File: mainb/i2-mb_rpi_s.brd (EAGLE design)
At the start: 110 x 110 mm, 30 parts, among them IC3 DS1307Z, T1 BC337, T2 BC337, X15 C-GRID-03-70543, X9 eth (mb->rpi)

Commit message: zmieniony ksztalt mainb
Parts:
- removed X1, X2, X3, X8: (no value), con-maritex:MICROMATCH-4
- removed X12, X13, X14: (no value), con-ptr500:AK500/3-H
- removed X4, X5, X6: (no value), con-ptr500:AK500/3
- added I2C_1, I2C_2, I2C_3, I2C_4: C-GRID-03-70553, con-molex:70553-03
- added PWR1, PWR2, PWR3: TBMP5103RC-KFV1, con-maritex:TBMP5103RC-KF
- moved U$8 23.3 mm to (20.3, 3.81)
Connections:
- net +12V_OUT: now also PWR1.3, PWR2.3, PWR3.3; no longer X4.3, X5.3, X6.3
- net +5V: now also PWR1.1, PWR2.1, PWR3.1; no longer X4.1, X5.1, X6.1
- net GND: now also I2C_1.3, I2C_2.3, I2C_3.3, I2C_4.3, PWR1.2, PWR2.2, PWR3.2; no longer X1.4, X12.2, X13.2, X14.2, X2.4, X3.4, X4.2, X5.2, X6.2, X8.4
- net SCL: now also I2C_1.2, I2C_2.2, I2C_3.2, I2C_4.2; no longer X1.3, X2.3, X3.3, X8.3
- net SDA: now also I2C_1.1, I2C_2.1, I2C_3.1, I2C_4.1; no longer X1.2, X2.2, X3.2, X8.2
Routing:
- net SDA: track 169.7 -> 28.0 mm
- net SCL: track 169.5 -> 31.6 mm
- net +5V_RPI: track 139.6 -> 2.54 mm, vias 1 -> 0
- net +5V: track 117.3 -> 0.00 mm
- net N$4: track 0.00 -> 88.4 mm
- net +12V_IN: track 64.8 -> 0.00 mm
- net +12V_OUT: track 47.5 -> 0.00 mm
- net TX+: track 24.1 -> 0.00 mm
- net TX-: track 24.0 -> 0.00 mm
- net RX+: track 23.9 -> 0.00 mm
- net RX-: track 23.7 -> 0.00 mm
- net AKU+: track 6.53 -> 0.00 mm
- removed copper zone on layer 1, net GND
- removed copper zone on layer 16, net GND
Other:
- board size 110 x 110 mm -> 110 x 107.6 mm

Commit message: 20-11-13 21:08
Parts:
- moved PWR2 211.1 mm to (26.9, 9.09), flipped to the bottom, turned to 60 degrees
- moved PWR1 153.8 mm to (-5.64, -27.8), flipped to the bottom, turned to 180 degrees
- moved I2C_3 136.5 mm to (8.75, -32.4), flipped to the bottom, turned to 180 degrees
- moved I2C_2 135.5 mm to (-23.7, 23.9), flipped to the bottom, turned to 300 degrees
- moved T2 126.2 mm to (14.2, -7.40), flipped to the bottom, turned to 180 degrees
- moved T1 116.3 mm to (-14.2, 8.00), flipped to the bottom
- moved PWR3 110.6 mm to (-26.9, 9.09), flipped to the bottom, turned to 300 degrees
- moved X15 108.1 mm to (-97.1, -87.0)
- moved R28 62.6 mm to (-13.6, 3.22), turned to 180 degrees
- moved BAT 61.2 mm to (42.1, -5.95), turned to 270 degrees
- moved IC3 61.1 mm to (55.7, -26.9)
- moved U$4 57.0 mm to (-10.2, 8.78), turned to 90 degrees
- moved U$8 49.9 mm to (-25.9, -15.0), turned to 180 degrees
- moved I2C_4 46.2 mm to (23.7, 23.9), flipped to the bottom, turned to 60 degrees
- moved Q2 39.4 mm to (25.9, -32.3)
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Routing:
- net N$4: track 88.4 -> 0.00 mm
- net SCL: track 31.6 -> 0.00 mm
- net SDA: track 28.0 -> 0.00 mm
- net N$3: track 25.2 -> 0.00 mm, vias 1 -> 0
- net GND: track 13.7 -> 0.00 mm, vias 3 -> 5
- net N$6: track 4.46 -> 0.00 mm
- net N$9: track 3.51 -> 0.00 mm
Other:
- board size 110 x 107.6 mm -> 110 x 106.6 mm

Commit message: 21.11.13 23:39
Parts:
- removed X15: C-GRID-03-70543, con-molex:70543-03
- added PWR4: C-GRID-03-70543, con-molex:70543-03
- I2C_1: value C-GRID-03-70553 -> C-GRID-03-70543; device con-molex:70553-03 -> con-molex:70543-03
- moved I2C_1 80.1 mm to (-31.8, -29.0), flipped to the bottom, turned to 270 degrees
- moved R2 43.3 mm to (7.20, -7.20), turned to 180 degrees
- moved R28 42.9 mm to (24.9, -15.8), turned to 90 degrees
- moved T1 42.0 mm to (23.0, -11.4), turned to 90 degrees
- moved R1 39.7 mm to (10.2, -7.20), turned to 180 degrees
- moved IC1 37.9 mm to (7.20, -10.8), turned to 180 degrees
- moved Q2 31.3 mm to (48.9, -11.1), turned to 90 degrees
- moved IC3 21.8 mm to (43.3, -9.06), turned to 90 degrees
- moved R3 8.96 mm to (23.4, -15.8), turned to 90 degrees
- moved U$4 8.81 mm to (-9.50, 0.00)
- moved U$3 7.03 mm to (9.50, 0.00), turned to 270 degrees
- moved T2 5.66 mm to (18.2, -11.4), turned to 90 degrees
- moved X9 3.62 mm to (-9.59, 24.4)
- moved X_ETH 1.60 mm to (0.00, 44.6)
- moved BAT 0.17 mm to (42.2, -5.80)
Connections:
- net +12V_OUT: now also PWR4.3; no longer X15.3
- net +5V: now also PWR4.1; no longer X15.1
- net GND: now also PWR4.2; no longer X15.2
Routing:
- net SCL: track 0.00 -> 200.5 mm, vias 0 -> 3
- net SDA: track 0.00 -> 184.4 mm
- net +5V: track 0.00 -> 121.6 mm, vias 0 -> 3
- net +12V_IN: track 0.00 -> 115.3 mm, vias 0 -> 1
- net +12V_OUT: track 0.00 -> 109.3 mm, vias 0 -> 1
- net +5V_RPI: track 2.54 -> 110.8 mm, vias 0 -> 1
- net AKU+: track 0.00 -> 59.7 mm, vias 1 -> 2
- net POE-: track 0.00 -> 51.6 mm, vias 0 -> 1
- net N$33: track 0.00 -> 42.5 mm, vias 0 -> 1
- net N$2: track 0.00 -> 29.7 mm
- net RX+: track 0.00 -> 27.3 mm, vias 0 -> 1
- net TX+: track 0.00 -> 27.0 mm, vias 0 -> 1
- net TX-: track 0.00 -> 22.2 mm, vias 0 -> 1
- net RX-: track 0.00 -> 21.1 mm
- net N$3: track 0.00 -> 19.8 mm
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- added copper zone on layer 1, net GND
- added copper zone on layer 16, net GND

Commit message: 22.11.13 17:00
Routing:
- net SCL: track 200.5 -> 183.5 mm
- net SDA: track 184.4 -> 187.6 mm
- net +5V: track 121.6 -> 120.5 mm
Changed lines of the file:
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@@
 <layer number="46" name="Milling" color="3" fill="1" visible="no" active="yes"/>
 <layer number="47" name="Measures" color="7" fill="1" visible="no" active="yes"/>
-<layer number="48" name="Document" color="7" fill="1" visible="no" active="yes"/>
+<layer number="48" name="Document" color="7" fill="1" visible="yes" active="yes"/>
 <layer number="49" name="Reference" color="7" fill="1" visible="yes" active="yes"/>
 <layer number="50" name="dxf" color="7" fill="1" visible="no" active="no"/>
@@
 <contactref element="I2C_3" pad="2"/>
 <contactref element="I2C_4" pad="2"/>
-<wire x1="-17.0808875" y1="20.049996875" x2="-8.6" y2="15.4" width="0.4064" layer="1"/>
-<wire x1="8.75" y1="-24.78" x2="8.75" y2="-23.45" width="0.4064" layer="16"/>
-<wire x1="7.3" y1="-22" x2="7.3" y2="-16.04" width="0.4064" layer="16"/>
-<wire x1="-8.6" y1="15.4" x2="8.6" y2="15.4" width="0.4064" layer="1" curve="-58.361612"/>
-<wire x1="17.0808875" y1="20.05" x2="8.6" y2="15.4" width="0.4064" layer="16"/>
-<via x="8.6" y="15.4" extent="1-16" drill="0.6"/>
-<wire x1="8.6" y1="15.4" x2="7.3" y2="-16.04" width="0.4064" layer="1" curve="-126.269"/>
-<wire x1="7.3" y1="-22" x2="8.75" y2="-23.45" width="0.4064" layer="16"/>
-<via x="7.3" y="-16.04" extent="1-16" drill="0.6"/>
 <contactref element="I2C_1" pad="2"/>
 <wire x1="-31.8" y1="-29" x2="-28.8" y2="-29" width="0.4064" layer="1"/>
@@
 <wire x1="6.25" y1="-9.4999" x2="6.25" y2="-10.65" width="0.3048" layer="1"/>
 <wire x1="6.25" y1="-10.65" x2="6.4" y2="-10.8" width="0.3048" layer="1"/>
-<wire x1="6.4" y1="-10.8" x2="13.8" y2="-10.8" width="0.3048" layer="1"/>
+<wire x1="6.4" y1="-10.8" x2="13.6" y2="-10.8" width="0.3048" layer="1"/>
 <wire x1="34.09" y1="-18.72" x2="34.09" y2="-17.11" width="0.4064" layer="1"/>
 <wire x1="34.09" y1="-17.11" x2="34.2" y2="-17" width="0.4064" layer="1"/>
 <wire x1="34.2" y1="-17" x2="37.8" y2="-17" width="0.4064" layer="1"/>
 <wire x1="37.8" y1="-17" x2="37.8" y2="-24.2" width="0.4064" layer="1"/>
-<wire x1="8.75" y1="-24.78" x2="8.75" y2="-35.85" width="0.4064" layer="16"/>
+<wire x1="8.75" y1="-24.78" x2="12.25" y2="-34.85" width="0.4064" layer="16"/>
 <wire x1="37.27" y1="-24.73" x2="27.52" y2="-24.73" width="0.4064" layer="1"/>
 <wire x1="0" y1="-37" x2="27.52" y2="-24.73" width="0.4064" layer="1" curve="48.0587"/>
@@
 <wire x1="37.8" y1="-8.8" x2="38.175" y2="-8.425" width="0.4064" layer="1"/>
 <wire x1="40.67" y1="-8.425" x2="38.175" y2="-8.425" width="0.4064" layer="1"/>
-<via x="8.75" y="-35.95" extent="1-16" drill="0.6"/>
-<wire x1="8.75" y1="-35.85" x2="8.75" y2="-35.95" width="0" layer="19" extent="16-16"/>
-<wire x1="6.4" y1="-10.8" x2="7.3" y2="-16.04" width="0" layer="19" extent="1-16"/>
-<wire x1="0" y1="-37" x2="8.75" y2="-35.95" width="0" layer="19" extent="1-1"/>
+<via x="12.25" y="-34.85" extent="1-16" drill="0.6"/>
+<wire x1="-17.0808875" y1="20.049996875" x2="-11.3" y2="13.2" width="0.4064" layer="1"/>
+<wire x1="17.0808875" y1="20.05" x2="11.3" y2="13.2" width="0.4064" layer="16"/>
+<wire x1="8.75" y1="-24.78" x2="5.82" y2="-16.37" width="0.4064" layer="16"/>
+<wire x1="-11.3" y1="13.2" x2="5.82" y2="-16.37" width="0.4064" layer="1" curve="-200.979"/>
+<via x="5.82" y="-16.37" extent="1-16" drill="0.6"/>
+<via x="11.3" y="13.2" extent="1-16" drill="0.6"/>
+<wire x1="-11.3" y1="13.2" x2="11.3" y2="13.2" width="0" layer="19" extent="1-16"/>
+<wire x1="6.4" y1="-10.8" x2="5.82" y2="-16.37" width="0" layer="19" extent="1-16"/>
+<wire x1="0" y1="-37" x2="12.25" y2="-34.85" width="0" layer="19" extent="1-1"/>
 </signal>
 <signal name="SDA">
@@
 <contactref element="I2C_3" pad="1"/>
 <contactref element="I2C_4" pad="1"/>
-<wire x1="6.21" y1="-24.78" x2="6.21" y2="-17.5650875" width="0.4064" layer="1"/>
-<wire x1="6.21" y1="-17.5650875" x2="6.21" y2="-12.1401" width="0.4064" layer="1"/>
-<wire x1="-15.8108875" y1="22.249703125" x2="-6.9" y2="17.3" width="0.4064" layer="1"/>
-<wire x1="18.3508875" y1="17.85029375" x2="12.1" y2="14.3" width="0.4064" layer="1"/>
-<wire x1="-6.9" y1="17.3" x2="6.21" y2="-17.5650875" width="0.4064" layer="1" curve="-182.32"/>
 <contactref element="I2C_1" pad="1"/>
 <wire x1="-31.8" y1="-26.46" x2="-27.74" y2="-26.46" width="0.4064" layer="1"/>
@@
 <wire x1="35.4" y1="-18.8" x2="35.4" y2="-20.2" width="0.4064" layer="1"/>
 <wire x1="35.4" y1="-20.2" x2="35.4" y2="-23.4" width="0.4064" layer="1"/>
-<wire x1="35.07" y1="-23.73" x2="26.92" y2="-23.73" width="0.4064" layer="1"/>
+<wire x1="35.07" y1="-23.73" x2="26.524365625" y2="-23.73" width="0.4064" layer="1"/>
 <wire x1="0" y1="-35.59" x2="26.5231375" y2="-23.731228125" width="0.4064" layer="1" curve="48.17983"/>
 <wire x1="35.07" y1="-23.73" x2="35.4" y2="-23.4" width="0.4064" layer="1"/>
-<wire x1="6.21" y1="-24.78" x2="6.21" y2="-34.99" width="0.4064" layer="1"/>
-<wire x1="6.21" y1="-34.99" x2="6.2" y2="-35" width="0.4064" layer="1"/>
+<wire x1="6.21" y1="-24.78" x2="8.61" y2="-34.49" width="0.4064" layer="1"/>
 <wire x1="33" y1="-20" x2="35.2" y2="-20" width="0.4064" layer="1"/>
 <wire x1="35.2" y1="-20" x2="35.4" y2="-20.2" width="0.4064" layer="1"/>
@@
 <wire x1="36.8" y1="-7.8" x2="37.445" y2="-7.155" width="0.4064" layer="1"/>
 <wire x1="40.67" y1="-7.155" x2="37.445" y2="-7.155" width="0.4064" layer="1"/>
-<wire x1="26.92" y1="-23.73" x2="26.524365625" y2="-23.73" width="0.4064" layer="1"/>
 <wire x1="26.524365625" y1="-23.73" x2="26.5231375" y2="-23.731228125" width="0.3048" layer="1"/>
-<wire x1="-6.9" y1="17.3" x2="12.1" y2="14.3" width="0" layer="19" extent="1-1"/>
-<wire x1="0" y1="-35.59" x2="6.21" y2="-34.99" width="0" layer="19" extent="1-1"/>
+<wire x1="-15.8108875" y1="22.249703125" x2="-10.8" y2="15.2" width="0.4064" layer="1"/>
+<wire x1="6.21" y1="-24.78" x2="4.6" y2="-18.2" width="0.4064" layer="1"/>
+<wire x1="-10.8" y1="15.2" x2="4.6" y2="-18.2" width="0.4064" layer="1" curve="-201.211"/>
+<wire x1="6.21" y1="-12.1401" x2="5.0599" y2="-12.1401" width="0.4064" layer="1"/>
+<wire x1="5.0599" y1="-12.1401" x2="4.6" y2="-12.6" width="0.4064" layer="1"/>
+<wire x1="4.6" y1="-12.6" x2="4.6" y2="-18.2" width="0.4064" layer="1"/>
+<wire x1="18.3508875" y1="17.85029375" x2="20.9" y2="13.5" width="0.4064" layer="1"/>
+<wire x1="20.9" y1="13.5" x2="15.8" y2="10.2" width="0.4064" layer="1"/>
+<wire x1="6.25" y1="-12.1001" x2="15.8" y2="10.2" width="0" layer="19" extent="1-1"/>
+<wire x1="0" y1="-35.59" x2="8.61" y2="-34.49" width="0" layer="19" extent="1-1"/>
 </signal>
 <signal name="N$41">
@@
 <contactref element="T1" pad="3"/>
 <wire x1="-9.5" y1="-0.85" x2="-9.5" y2="-5" width="0.4064" layer="1"/>
-<wire x1="1.4" y1="-12.8" x2="1.41" y2="-8.6" width="0.4064" layer="1"/>
+<wire x1="1.4" y1="-12.8" x2="1.4" y2="-8.6" width="0.4064" layer="1"/>
 <via x="1.4" y="-12.8" extent="1-16" drill="0.6"/>
 <wire x1="-9.5" y1="-5" x2="-7.2" y2="-5" width="0.4064" layer="1"/>
-<wire x1="-7.2" y1="-5" x2="1.41" y2="-8.6" width="0.4064" layer="1" curve="64.4683"/>
+<wire x1="-7.2" y1="-5" x2="1.4" y2="-8.6" width="0.4064" layer="1" curve="64.4683"/>
 <wire x1="21.77" y1="-13.9" x2="2.5" y2="-13.9" width="0.4064" layer="16"/>
 <wire x1="2.5" y1="-13.9" x2="1.4" y2="-12.8" width="0.4064" layer="16"/>
@@
 <contactref element="PWR2" pad="1"/>
 <contactref element="PWR1" pad="1"/>
-<wire x1="-10.72" y1="-27.8" x2="-10.72" y2="-34.12" width="0.8128" layer="1"/>
-<wire x1="29.43" y1="4.690590625" x2="34.9" y2="7.9" width="0.8128" layer="16"/>
-<wire x1="-10.72" y1="-34.12" x2="34.9" y2="7.9" width="0.8128" layer="16" curve="-239.803468"/>
-<via x="-10.72" y="-34.12" extent="1-16" drill="0.6"/>
+<wire x1="-10.72" y1="-27.8" x2="-12.82" y2="-33.32" width="0.8128" layer="1"/>
+<wire x1="29.43" y1="4.690590625" x2="35.2" y2="5.6" width="0.8128" layer="16"/>
+<wire x1="-12.82" y1="-33.32" x2="35.2" y2="5.6" width="0.8128" layer="16" curve="-239.803468"/>
+<via x="-12.82" y="-33.32" extent="1-16" drill="0.6"/>
 <wire x1="-24.35" y1="13.48940625" x2="-31.2" y2="17.4" width="0.8128" layer="1"/>
 <via x="-31.2" y="17.4" extent="1-16" drill="0.6"/>
@@
 <via x="-35.2" y="-16.2" extent="1-16" drill="0.6"/>
 <wire x1="-35.2" y1="-16.2" x2="-32" y2="-16.2" width="0.8128" layer="16"/>
-<wire x1="-10.72" y1="-27.8" x2="-32" y2="-16.2" width="0" layer="19" extent="16-16"/>
+<wire x1="-12.82" y1="-33.32" x2="-35.2" y2="-31" width="0" layer="19" extent="1-1"/>
 <wire x1="-24.35" y1="13.48940625" x2="-32" y2="-16.2" width="0" layer="19" extent="16-16"/>
 </signal>
@@
 <wire x1="7.2" y1="-12.0999" x2="7.2" y2="-13" width="0.3048" layer="1"/>
 <wire x1="7.2" y1="-13" x2="7.4" y2="-13.2" width="0.3048" layer="1"/>
-<wire x1="7.4" y1="-13.2" x2="9.8" y2="-13.2" width="0.3048" layer="1"/>
-<wire x1="9.8" y1="-13.2" x2="10" y2="-13" width="0.3048" layer="1"/>
-<via x="10" y="-13" extent="1-16" drill="0.6"/>
-<wire x1="10" y1="-13" x2="10" y2="-11.4" width="0.3048" layer="16"/>
-<wire x1="10" y1="-11.4" x2="9.8" y2="-11.2" width="0.3048" layer="16"/>
-<wire x1="9.8" y1="-11.2" x2="0" y2="-11.2" width="0.3048" layer="16"/>
+<wire x1="7.4" y1="-13.2" x2="9.4" y2="-13.2" width="0.3048" layer="1"/>
+<wire x1="9.4" y1="-13.2" x2="9.9" y2="-12.7" width="0.3048" layer="1"/>
+<via x="9.9" y="-12.7" extent="1-16" drill="0.6"/>
+<wire x1="9.9" y1="-12.7" x2="9.9" y2="-11.4" width="0.3048" layer="16"/>
+<wire x1="9.9" y1="-11.4" x2="9.7" y2="-11.2" width="0.3048" layer="16"/>
+<wire x1="9.7" y1="-11.2" x2="0" y2="-11.2" width="0.3048" layer="16"/>
 <wire x1="40.67" y1="-10.965" x2="42.765" y2="-10.965" width="0.4064" layer="1"/>
 <wire x1="42.765" y1="-10.965" x2="43.2" y2="-11.4" width="0.4064" layer="1"/>

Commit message: 26.11 10:46
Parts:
- added C1: 100n, rcl:C0603
- added LED1, LED2, LED3: (no value), wb:D0603
- added R4, R5, R6: 500, rcl:R0603
- added R7: (no value), rcl:R0603
- U$2: device RaspberryPi:RASPBERRY-PI_REV1_HOLES -> RaspberryPi:RASPBERRY-PI_HOLES
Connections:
- new net LED2: LED2.2, U$2.16
- new net LED3: LED3.2, U$2.18
- new net N$10: IC3.7, R7.2
- new net N$4: LED2.1, R5.1
- new net N$5: LED1.1, R4.1
- new net N$7: LED1.2, U$2.22
- new net N$8: LED3.1, R6.1
- net +5V_RPI: now also C1.1, R4.2, R5.2, R6.2, R7.1
- net GND: now also C1.2
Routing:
- net N$7: track 0.00 -> 25.7 mm, vias 0 -> 1
- net LED3: track 0.00 -> 19.0 mm, vias 0 -> 1
- net +5V_RPI: track 110.4 -> 129.3 mm
- net LED2: track 0.00 -> 15.1 mm, vias 0 -> 1
- net N$10: track 0.00 -> 10.6 mm
- net N$8: track 0.00 -> 1.30 mm
- net N$5: track 0.00 -> 1.30 mm
- net N$4: track 0.00 -> 1.30 mm

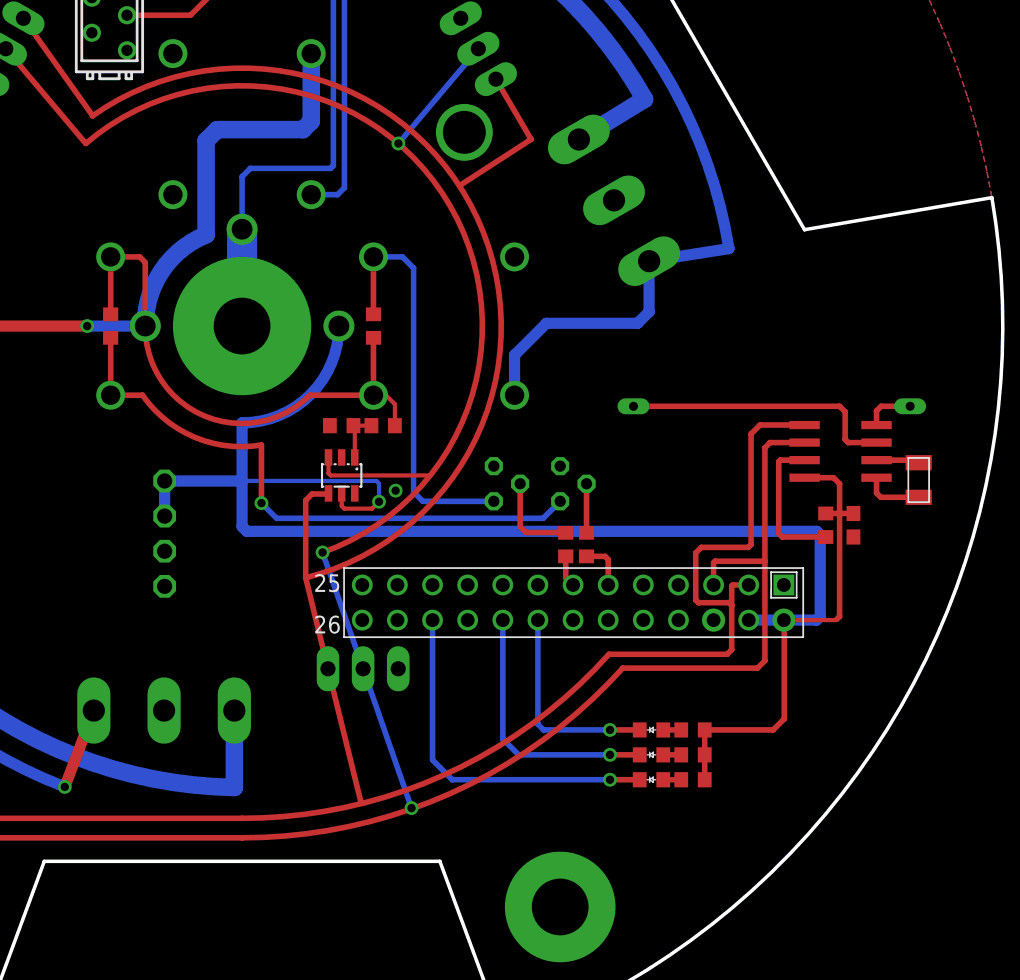
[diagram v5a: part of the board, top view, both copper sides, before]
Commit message: RPi camera board added and library, added servos.lbr
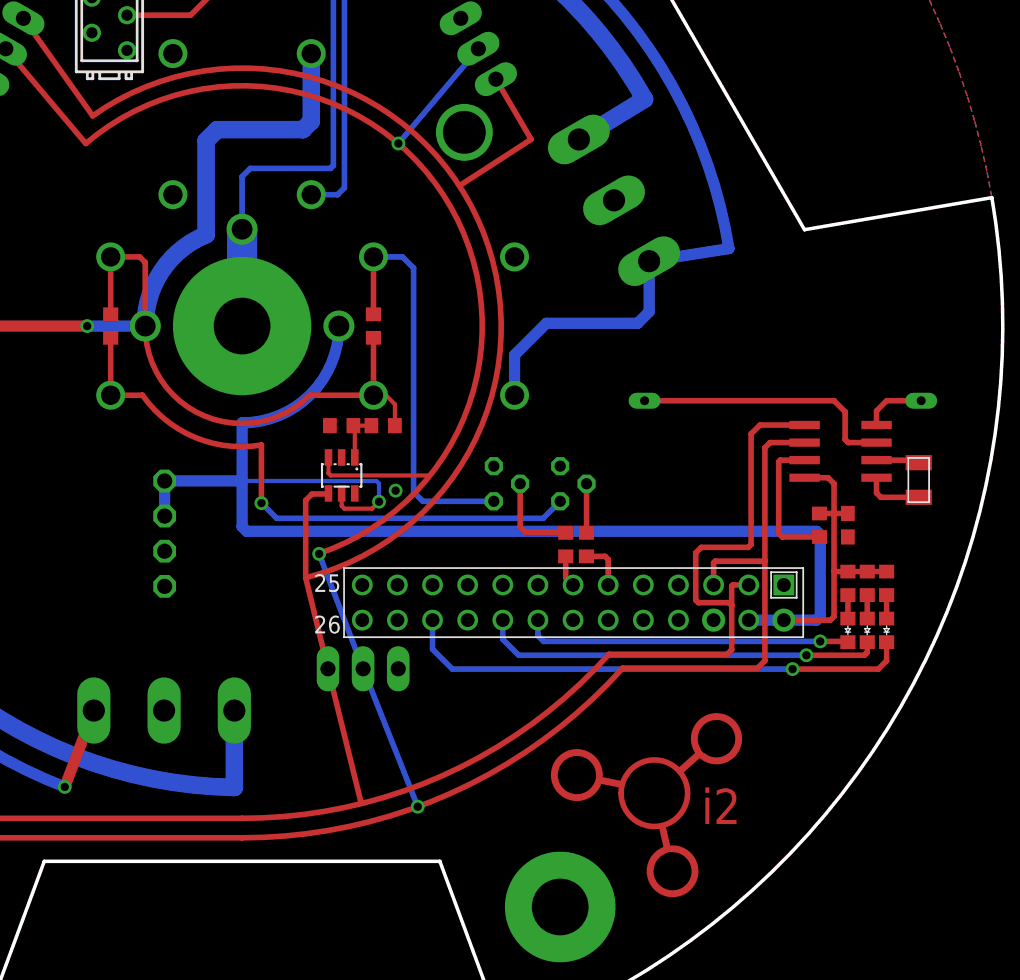
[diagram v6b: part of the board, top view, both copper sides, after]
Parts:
- moved LED1 20.1 mm to (46.6, -22.0), turned to 270 degrees
- moved R4 19.9 mm to (46.6, -18.6), turned to 90 degrees
- moved LED3 18.0 mm to (45.2, -22.0), turned to 270 degrees
- moved R6 17.7 mm to (45.2, -18.6), turned to 90 degrees
- moved LED2 15.9 mm to (43.8, -22.0), turned to 270 degrees
- moved R5 15.4 mm to (43.8, -18.6), turned to 90 degrees
- moved BAT 0.89 mm to (43.0, -5.40)
- moved R7 0.45 mm to (41.8, -14.4)
- moved C1 0.40 mm to (43.8, -14.4)
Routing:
- net +5V_RPI: track 129.3 -> 115.6 mm
- net N$7: track 25.7 -> 37.1 mm
- net LED3: track 19.0 -> 29.0 mm
- net LED2: track 15.1 -> 23.8 mm
- net LOGO: track 0.00 -> 6.78 mm
- net GND: track 3.59 -> 4.56 mm
- net N$3: track 19.8 -> 19.2 mm
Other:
- board text added: "i2"
